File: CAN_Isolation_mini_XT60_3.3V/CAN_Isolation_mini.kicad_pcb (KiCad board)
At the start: 4 copper layers, 60 x 70 mm, 60 parts, among them J1 S4B-XH-A, J10 Conn_01x04_Pin, J11 Conn_01x04_Pin, J12 Conn_01x04_Pin, J13 Conn_01x04_Pin, J14 Conn_01x04_Pin, J15 Conn_01x04_Pin, J16 Conn_01x04_Pin, J17 Conn_01x04_Pin, J2 Conn_01x04_Pin, J21 XT60PW-F, J22 XT60PW-F, J3 Conn_01x04_Pin, J4 Conn_01x04_Pin, J5 Conn_01x04_Pin, J6 Conn_01x04_Pin, J7 Conn_01x04_Pin, J8 Conn_01x04_Pin, J9 Conn_01x04_Pin, U1 MCP2518FDT-H/SL, U2 ISO1042QDWVRQ1, U3 MGS3123R3, U4 MGS1R51205, U5 TVS1800DRVR, U6 DTC114ECAHZGT116, U7 MGS102405, Y1 CSTNE20M0V530000R0

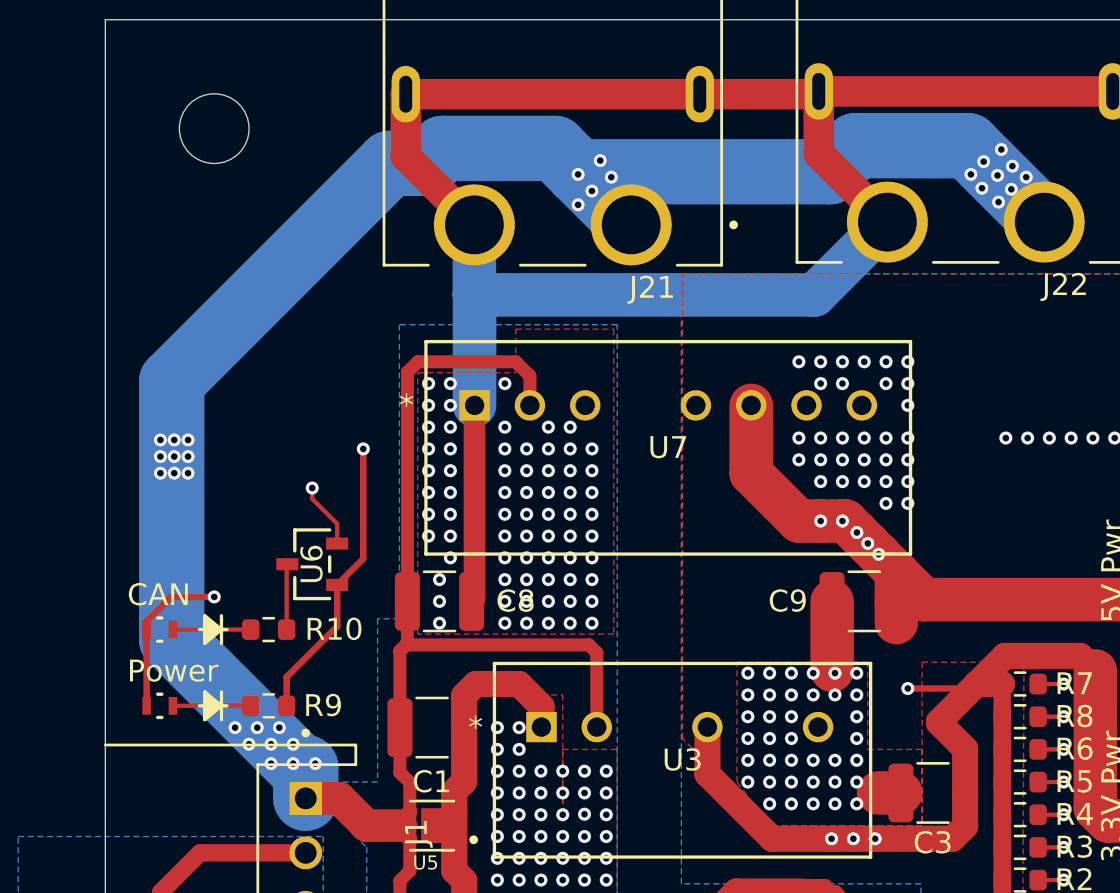
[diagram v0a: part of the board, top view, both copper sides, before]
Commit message: Add diode for servo line.
Add diode for servo line.
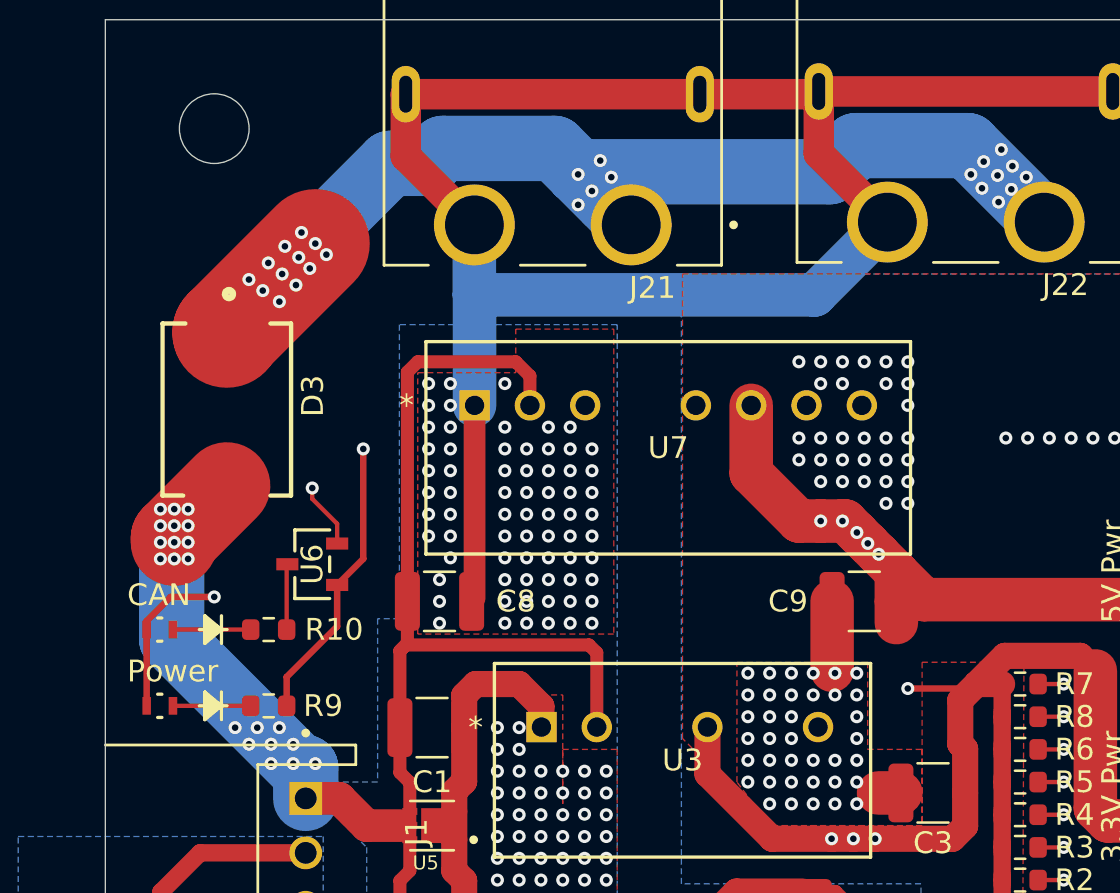
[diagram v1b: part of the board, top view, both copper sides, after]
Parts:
- added D3: B520CQ-13-F, CAN_Isolation:DIOM7959X250N, F.Cu at (94.2, 75.7)
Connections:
- J21 pad 1: BAT_12V -> Net-(D3-PadC)
- J22 pad 1: BAT_12V -> Net-(D3-PadC)
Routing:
- net BAT_12V: track 283.6 -> 100.4 mm, vias 32 -> 21
- net Net-(D3-PadC): track 0.00 -> 139.9 mm, vias 0 -> 26
- net +3.3VP: track 202.1 -> 201.3 mm

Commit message: Change board size.
Change board size.
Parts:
- moved G*** 50.1 mm to (136.5, 122.7)
- moved REF** 10.0 mm to (143.7, 72.8)
- moved REF** 10.0 mm to (93.7, 72.8)
- moved J22 9.32 mm to (127.2, 76.4)
- moved J21 9.11 mm to (109.2, 76.3)
- moved U7 6.24 mm to (105.6, 81.7)
- moved C8 6.06 mm to (103.6, 90.6)
- moved D3 5.83 mm to (95.9, 81.3), turned to 180 degrees
- moved C9 5.50 mm to (129.0, 84.7)
- moved C1 4.60 mm to (103.7, 94.9)
- moved U5 4.60 mm to (103.7, 99.4)
- moved U6 3.91 mm to (99.4, 86.5)
- moved C11 3.51 mm to (100.2, 115.3)
- moved C12 3.51 mm to (100.2, 117.3)
- moved C2 3.51 mm to (103.7, 103.3)
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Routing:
- net BAT_GND: track 149.9 -> 113.2 mm, vias 163 -> 167
- net BAT_12V: track 100.4 -> 118.0 mm, vias 21 -> 25
- net Net-(D3-PadC): track 139.9 -> 125.7 mm, vias 26 -> 16
- net CAN_LED: track 93.3 -> 106.2 mm
- net GND_VP: track 89.3 -> 95.9 mm, vias 109 -> 107
- net +3.3VP: track 201.3 -> 197.7 mm
- net CAN_L: track 44.7 -> 48.2 mm
- net +5VP: track 66.7 -> 70.1 mm
- net GND_5VCAN: track 18.2 -> 21.4 mm, vias 186 -> 183
- net CAN_SCK: track 31.7 -> 29.7 mm
- net CAN_SDI: track 27.0 -> 25.6 mm
- net CAN_H: track 56.4 -> 57.9 mm
- net Net-(R10-Pad2): track 3.01 -> 1.78 mm
- net Net-(LED2-Pad1): track 3.57 -> 4.37 mm
- net CAN_SDO: track 23.2 -> 22.6 mm
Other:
- board size 60 x 70 mm -> 60 x 60 mm

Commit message: Fix XT60 line.
Fix XT60 line.
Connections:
- J22 pad 1: Net-(D3-PadC) -> BAT_12V
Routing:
- net BAT_12V: track 118.0 -> 210.2 mm
- net Net-(D3-PadC): track 125.7 -> 64.3 mm
- net BAT_GND: vias 167 -> 166
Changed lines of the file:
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@@
 			(layers "*.Cu" "*.Mask")
 			(remove_unused_layers no)
-			(net 59 "Net-(D3-PadC)")
+			(net 1 "BAT_12V")
 			(pinfunction "1")
 			(pintype "passive")
@@
 	)
 	(segment
+		(start 128.3236 73.8466)
+		(end 122.594744 73.8466)
+		(width 1)
+		(layer "B.Cu")
+		(net 1)
+	)
+	(segment
+		(start 92.075 86.614)
+		(end 92.075 83.61)
+		(width 3)
+		(layer "B.Cu")
+		(net 1)
+	)
+	(segment
+		(start 98.717454 84.0954)
+		(end 98.123654 83.5016)
+		(width 1)
+		(layer "B.Cu")
+		(net 1)
+	)
+	(segment
+		(start 102.33 82.183946)
+		(end 100.418546 84.0954)
+		(width 1)
+		(layer "B.Cu")
+		(net 1)
+	)
+	(segment
+		(start 103.43 79.19)
+		(end 102.33 80.29)
+		(width 1)
+		(layer "B.Cu")
+		(net 1)
+	)
+	(segment
+		(start 92.1834 83.5016)
+		(end 92.075 83.61)
+		(width 1)
+		(layer "B.Cu")
+		(net 1)
+	)
+	(segment
+		(start 122.594744 73.8466)
+		(end 116.587944 79.8534)
+		(width 1)
+		(layer "B.Cu")
+		(net 1)
+	)
+	(segment
+		(start 100.418546 84.0954)
+		(end 98.717454 84.0954)
+		(width 1)
+		(layer "B.Cu")
+		(net 1)
+	)
+	(segment
 		(start 97.595905 92.134905)
 		(end 92.075 86.614)
@@
 	)
 	(segment
+		(start 102.33 80.29)
+		(end 102.33 82.183946)
+		(width 1)
+		(layer "B.Cu")
+		(net 1)
+	)
+	(segment
 		(start 97.857095 92.134905)
 		(end 97.595905 92.134905)
@@
 	)
 	(segment
-		(start 92.075 86.614)
+		(start 116.587944 79.8534)
+		(end 107.605088 79.8534)
+		(width 1)
+		(layer "B.Cu")
+		(net 1)
+	)
+	(segment
+		(start 130.835 76.358)
+		(end 128.3236 73.8466)
+		(width 1)
+		(layer "B.Cu")
+		(net 1)
+	)
+	(segment
+		(start 92.075 83.61)
 		(end 92.075 79.883)
 		(width 3)
@@
 	)
 	(segment
+		(start 106.941688 79.19)
+		(end 103.43 79.19)
+		(width 1)
+		(layer "B.Cu")
+		(net 1)
+	)
+	(segment
 		(start 97.857095 93.544905)
 		(end 97.857095 92.134905)
@@
 	)
 	(segment
+		(start 98.123654 83.5016)
+		(end 92.1834 83.5016)
+		(width 1)
+		(layer "B.Cu")
+		(net 1)
+	)
+	(segment
+		(start 107.605088 79.8534)
+		(end 106.941688 79.19)
+		(width 1)
+		(layer "B.Cu")
+		(net 1)
+	)
+	(segment
 		(start 92.075 82.042)
 		(end 92.075 80.391)
@@
 	)
 	(segment
+		(start 100.332968 84.1954)
+		(end 98.549032 84.1954)
+		(width 1.2)
+		(layer "In2.Cu")
+		(net 1)
+	)
+	(segment
+		(start 108.763667 79.9534)
+		(end 107.950267 79.14)
+		(width 1.2)
+		(layer "In2.Cu")
+		(net 1)
+	)
+	(segment
+		(start 102.4446 80.304667)
+		(end 102.4446 82.083768)
+		(width 1.2)
+		(layer "In2.Cu")
+		(net 1)
+	)
+	(segment
 		(start 97.857095 92.396095)
 		(end 95.123 89.662)
@@
 	)
 	(segment
+		(start 119.8534 73.7466)
+		(end 113.6466 79.9534)
+		(width 1.2)
+		(layer "In2.Cu")
+		(net 1)
+	)
+	(segment
 		(start 92.202 86.741)
 		(end 92.202 85.852)
@@
 	)
 	(segment
+		(start 107.950267 79.14)
+		(end 103.609267 79.14)
+		(width 1.2)
+		(layer "In2.Cu")
+		(net 1)
+	)
+	(segment
+		(start 92.202 83.6)
+		(end 92.202 80.518)
+		(width 2.8)
+		(layer "In2.Cu")
+		(net 1)
+	)
+	(segment
 		(start 97.857095 93.544905)
 		(end 97.857095 93.158095)
@@
 	)
 	(segment
+		(start 97.755232 83.4016)
+		(end 92.4004 83.4016)
+		(width 1.2)
+		(layer "In2.Cu")
+		(net 1)
+	)
+	(segment
+		(start 113.6466 79.9534)
+		(end 108.763667 79.9534)
+		(width 1.2)
+		(layer "In2.Cu")
+		(net 1)
+	)
+	(segment
 		(start 97.857095 93.158095)
 		(end 97.857095 92.396095)
@@
 	)
 	(segment
+		(start 98.549032 84.1954)
+		(end 97.755232 83.4016)
+		(width 1.2)
+		(layer "In2.Cu")
+		(net 1)
+	)
+	(segment
+		(start 102.4446 82.083768)
+		(end 100.332968 84.1954)
+		(width 1.2)
+		(layer "In2.Cu")
+		(net 1)
+	)
+	(segment
+		(start 92.4004 83.4016)
+		(end 92.202 83.6)
+		(width 1.2)
+		(layer "In2.Cu")
+		(net 1)
+	)
+	(segment
+		(start 130.835 76.358)
+		(end 128.2236 73.7466)
+		(width 1.2)
+		(layer "In2.Cu")
+		(net 1)
+	)
+	(segment
+		(start 103.609267 79.14)
+		(end 102.4446 80.304667)
+		(width 1.2)
+		(layer "In2.Cu")
+		(net 1)
+	)
+	(segment
+		(start 128.2236 73.7466)
+		(end 119.8534 73.7466)
+		(width 1.2)
+		(layer "In2.Cu")
+		(net 1)
+	)
+	(segment
 		(start 92.202 85.852)
-		(end 92.202 80.518)
+		(end 92.202 83.6)
 		(width 2.8)
 		(layer "In2.Cu")
@@
 	)
 	(via
-		(at 108 78.9)
-		(size 0.6)
-		(drill 0.3)
-		(layers "F.Cu" "B.Cu")
-		(net 2)
-	)
-	(via
 		(at 109.657095 98.809)
 		(size 0.6)
@@
 	)
 	(segment
-		(start 121.663951 73.5046)
-		(end 122.270551 72.898)
-		(width 2.8)
-		(layer "F.Cu")
-		(net 59)
-	)
-	(segment
-		(start 116.336822 73.5046)
-		(end 118.11 73.5046)
-		(width 2.8)
-		(layer "F.Cu")
-		(net 59)
-	)
-	(segment
 		(start 99.388363 81.28)
 		(end 99.388363 79.074162)
@@
 	)
 	(segment
-		(start 122.270551 72.898)
-		(end 125.095 72.898)
-		(width 2.8)
-		(layer "F.Cu")
-		(net 59)
-	)
-	(segment
-		(start 129.413 74.676)
-		(end 130.835 76.098)
-		(width 2.8)
-		(layer "F.Cu")
-		(net 59)
-	)
-	(segment
-		(start 113.514422 76.327)
-		(end 116.336822 73.5046)
-		(width 2.8)
-		(layer "F.Cu")
-		(net 59)
-	)
-	(segment
 		(start 104.16213 72.8)
 		(end 109.274 72.8)
@@
 	)
 	(segment
-		(start 127.635 72.898)
-		(end 129.413 74.676)
-		(width 2.8)
-		(layer "F.Cu")
-		(net 59)
-	)
-	(segment
-		(start 118.11 73.5046)
-		(end 121.663951 73.5046)
-		(width 2.8)
-		(layer "F.Cu")
-		(net 59)
-	)
-	(segment
-		(start 125.095 72.898)
-		(end 127.635 72.898)
-		(width 2.8)
-		(layer "F.Cu")
-		(net 59)
-	)
-	(segment
 		(start 99.5534 77.40873)
 		(end 104.16213 72.8)
@@
 	)
 	(segment
-		(start 112.801 76.327)
-		(end 115.722 73.406)
-		(width 2.8)
-		(layer "B.Cu")
-		(net 59)
-	)
-	(segment
-		(start 115.722 73.406)
-		(end 116.332 73.406)
-		(width 2.8)
-		(layer "B.Cu")
-		(net 59)
-	)
-	(segment
 		(start 112.776 76.327)
 		(end 112.801 76.327)
@@
 	)
 	(segment
-		(start 127.4296 72.9466)
-		(end 128.778 74.295)
-		(width 2.8)
-		(layer "B.Cu")
-		(net 59)
-	)
-	(segment
 		(start 99.568 82.042)
 		(end 99.568 77.535551)
@@
 	)
 	(segment
-		(start 116.332 73.406)
-		(end 121.762551 73.406)
-		(width 2.8)
-		(layer "B.Cu")
-		(net 59)
-	)
-	(segment
 		(start 99.568 77.535551)
 		(end 104.187951 72.9156)
@@
 	)
 	(segment
-		(start 122.221951 72.9466)
-		(end 127.4296 72.9466)
-		(width 2.8)
-		(layer "B.Cu")
-		(net 59)
-	)
-	(segment
-		(start 121.762551 73.406)
-		(end 122.221951 72.9466)
-		(width 2.8)
-		(layer "B.Cu")
-		(net 59)
-	)
-	(segment
-		(start 128.778 74.295)
-		(end 130.835 76.352)
-		(width 2.8)
-		(layer "B.Cu")
-		(net 59)
-	)
-	(segment
 		(start 109.3646 72.9156)
 		(end 112.776 76.327)
@@
 	)
 	(segment
-		(start 127.248 72.771)
-		(end 130.835 76.358)
-		(width 2.8)
-		(layer "In2.Cu")
-		(net 59)
-	)
-	(segment
 		(start 100.965 75.565)
 		(end 99.4534 77.0766)
@@
 	)
 	(segment
-		(start 116.5184 73.2114)
-		(end 121.4796 73.2114)
-		(width 2.8)
-		(layer "In2.Cu")
-		(net 59)
-	)
-	(segment
 		(start 99.4534 77.0766)
 		(end 99.4534 78.486)
@@
 	)
 	(segment
-		(start 121.92 72.771)
-		(end 127.248 72.771)
-		(width 2.8)
-		(layer "In2.Cu")
-		(net 59)
-	)
-	(segment
 		(start 112.801 76.327)
 		(end 112.395 76.327)
@@
 	)
 	(segment
-		(start 116.459 73.152)
-		(end 116.5184 73.2114)
-		(width 2.8)
-		(layer "In2.Cu")
-		(net 59)
-	)
-	(segment
-		(start 121.4796 73.2114)
-		(end 121.92 72.771)
-		(width 2.8)
-		(layer "In2.Cu")
-		(net 59)
-	)
-	(segment
 		(start 105.029 72.9156)
 		(end 103.6144 72.9156)
@@
 		(width 2.8)
 		(layer "In2.Cu")
-		(net 59)
-	)
-	(segment
-		(start 113.284 76.327)
-		(end 116.459 73.152)
-		(width 2.8)
-		(layer "In2.Cu")

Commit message: Change connector.
Change connector.
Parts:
- added X1: B2PS-VH, CAN_Isolation:B2PS-VH, F.Cu at (97.9, 95.9)
- J1: value S4B-XH-A -> S2B-XH-A; footprint CAN_Isolation:JST_S4B-XH-A -> CAN_Isolation:JST_S2B-XH-A
- moved J1 7.86 mm to (92.0, 105.2)
- moved D1 3.79 mm to (92.0, 111.6)
- moved C10 3.32 mm to (91.9, 115.1)
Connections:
- J1 pad 1: BAT_12V -> CAN_H
- J1 pad 2: CAN_H -> CAN_L
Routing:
- net CAN_L: track 48.2 -> 32.1 mm
- net GND_5VCAN: track 21.4 -> 27.4 mm, vias 183 -> 180
- net CAN_H: track 57.9 -> 52.5 mm
- net BAT_GND: vias 166 -> 171
